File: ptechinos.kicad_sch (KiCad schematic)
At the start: 73 parts, among them J1 B+, J2 Battery, J3 B-, J4 AudioJack4, J5 Trackpad FPC, J6 OLED, SW1 SW_Power, SW2 Reset, U1 ProMicro

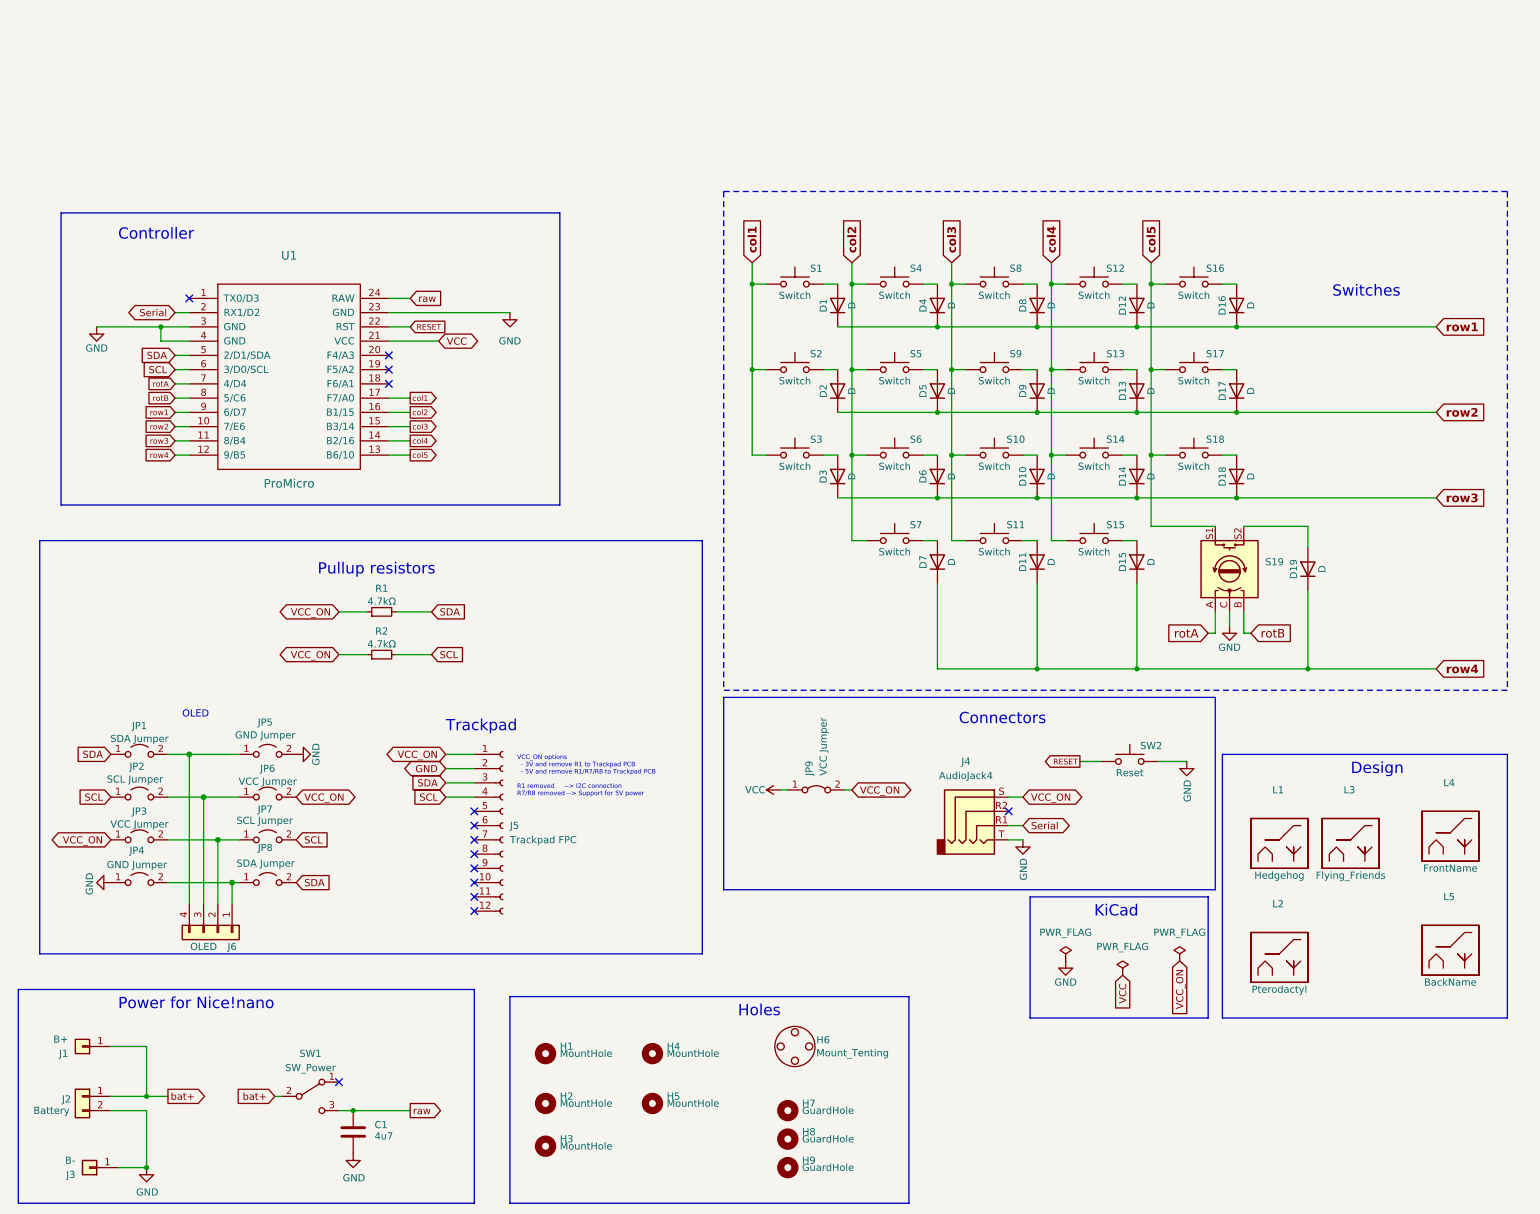
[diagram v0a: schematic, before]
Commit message: ✨ 💥 🚧 - Add another position for the encoder / key. Adjust matrix accordingly. Note that encoder A/B lines are currently shared. Update both schematic and PCB to fit all. Adjust board to 62c46e3cfa2ad35a7dbc6e8ceb0ca2087bb40a82 and 578a124142dade73bf22a96b8bd2c4353eafd8da.
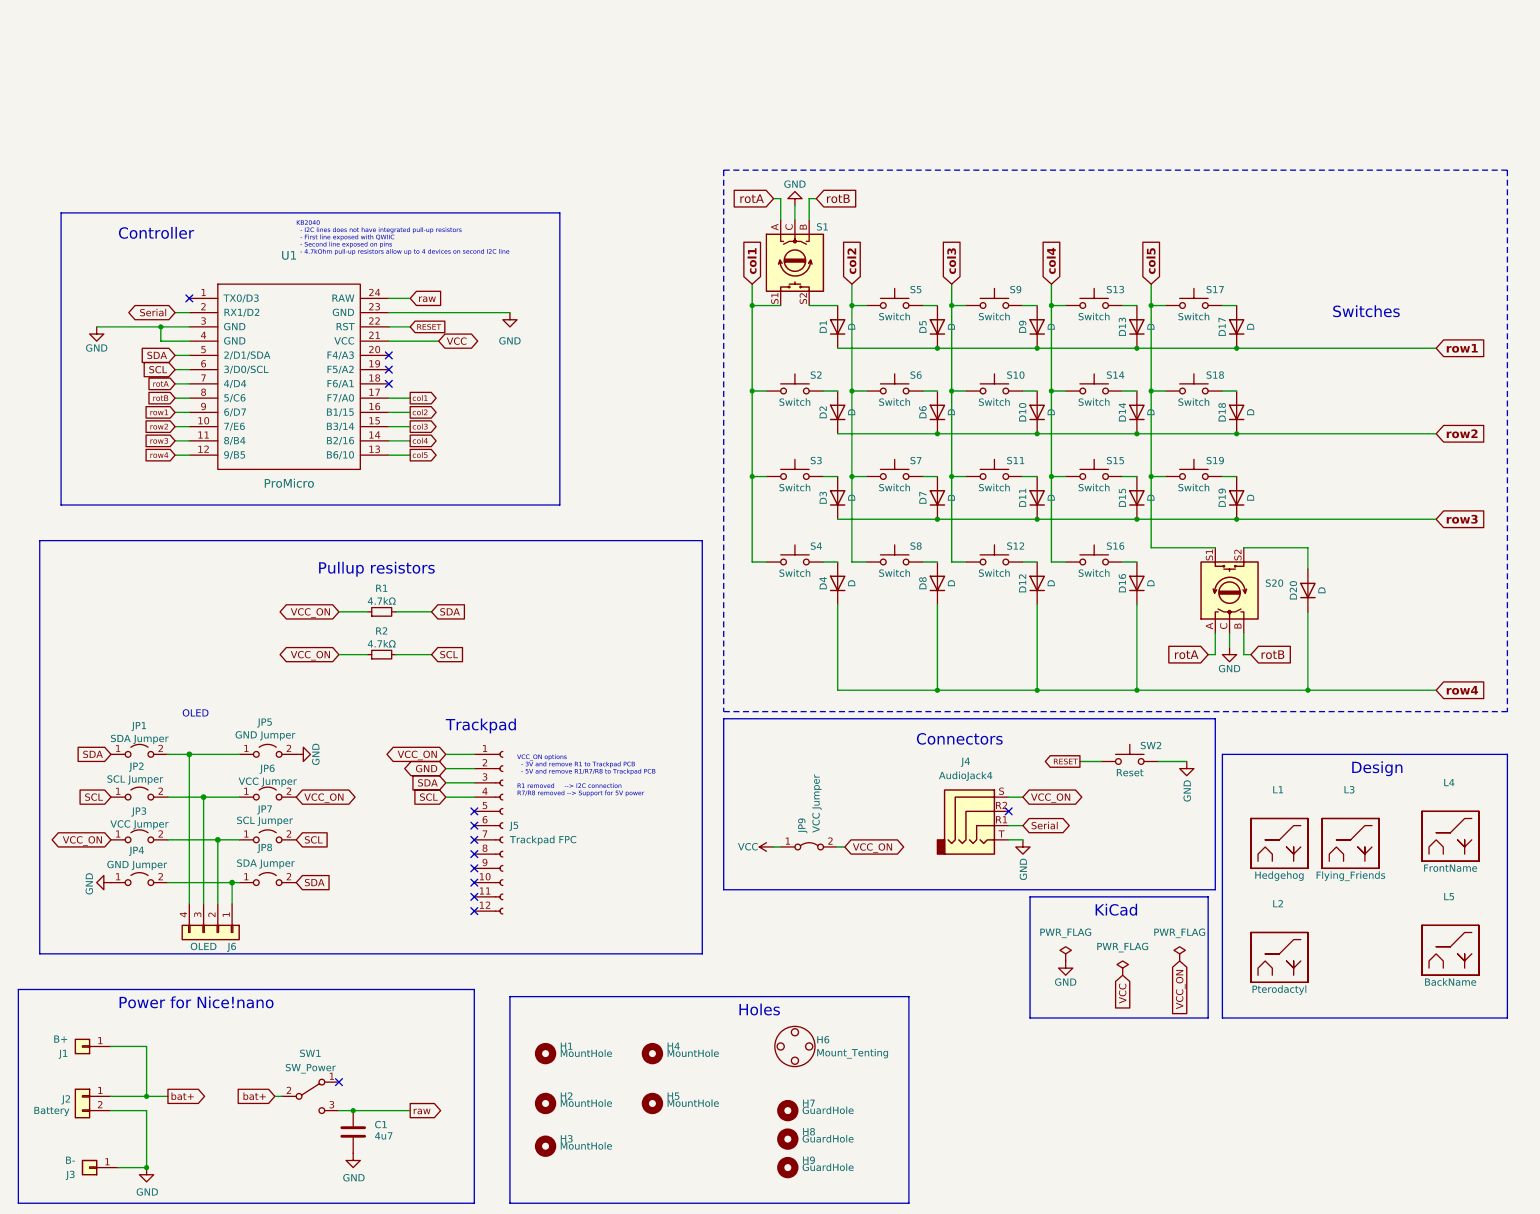
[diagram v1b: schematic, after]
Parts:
- removed S1: Switch, ptechinos:Kailh_socket_PG1350_optional_reversible.kicad_mod, symbol Switch:SW_Push
- added D4: D, ptechinos:D3_TH_SMD_v2, symbol Device:D
- added S1: RotaryEncoder_Switch, ptechinos:pg1350-EVQWGD001_R, symbol Device:RotaryEncoder_Switch
- added S4: Switch, ptechinos:Kailh_socket_PG1350_optional_reversible.kicad_mod, symbol Switch:SW_Push
- renumbered D9 to D10, D10 to D11, D11 to D12, D12 to D13, D13 to D14, D14 to D15, D15 to D16, D16 to D17, D17 to D18, D18 to D19, D19 to D20, D4 to D5, D5 to D6, D6 to D7, D7 to D8, D8 to D9, S9 to S10, S10 to S11, S11 to S12, S12 to S13, S13 to S14, S14 to S15, S15 to S16, S16 to S17, S17 to S18, S18 to S19, S19 to S20, S4 to S5, S5 to S6, S6 to S7, S7 to S8, S8 to S9
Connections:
- net GND: now also S1.C
- net col1: now also S1.S1, S4.1
- net rotA: now also S1.A
- net rotB: now also S1.B
- net row4: now also D4.1 (K)
- net at D1.2 (A): now also S1.S2
- new net: D4.2 (A), S4.2
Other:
- note added: "KB2040 - I2C lines does not have integrated pull-up resistors - First line exposed with QWIIC - Second line exposed on pins - 4.7kOhm pull-up resistors allow up to 4 devices on second I2C line"
- moved on the sheet: D1, D10, D11, D12, D13, D14, D15, D16, D17, D18, D19, D2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

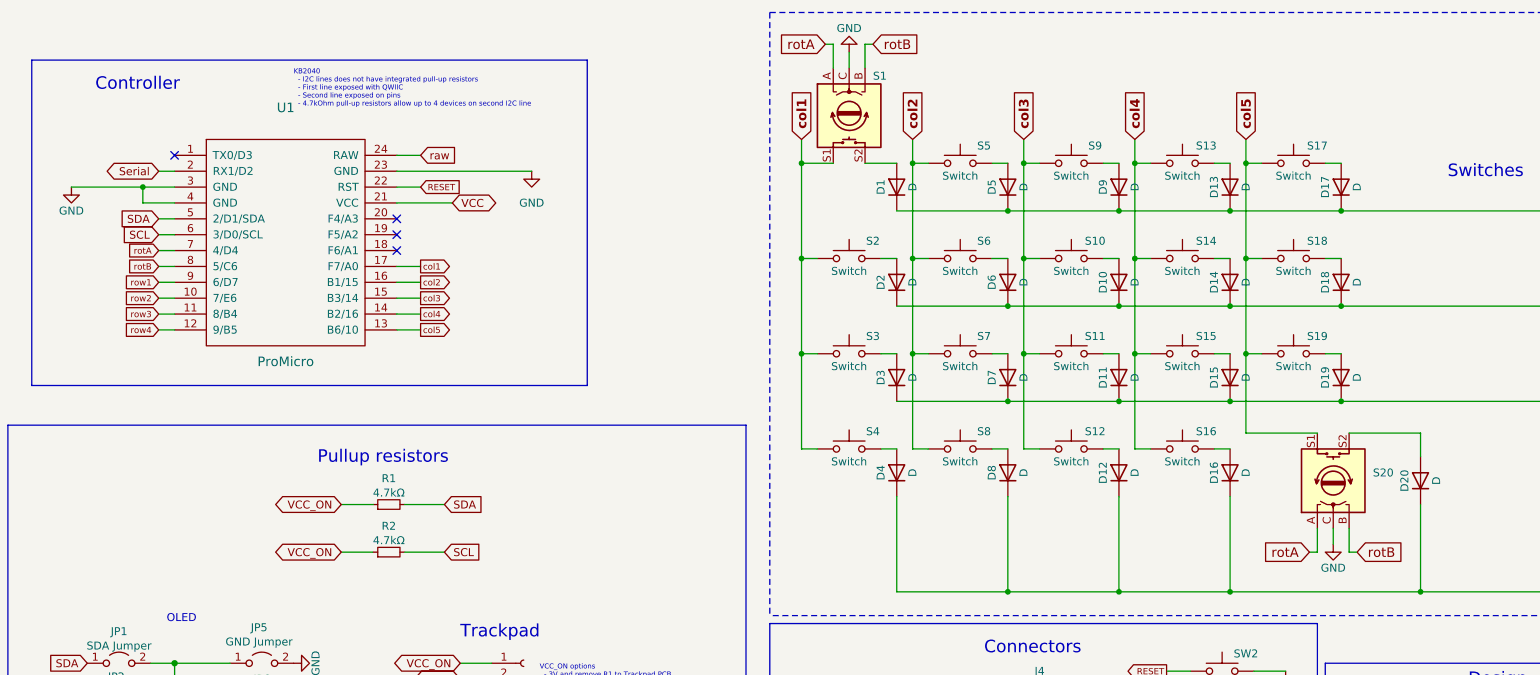
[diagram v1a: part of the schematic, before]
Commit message: ✨ 💥 - Both encoders (top and thumbs) are now using distinct pins.
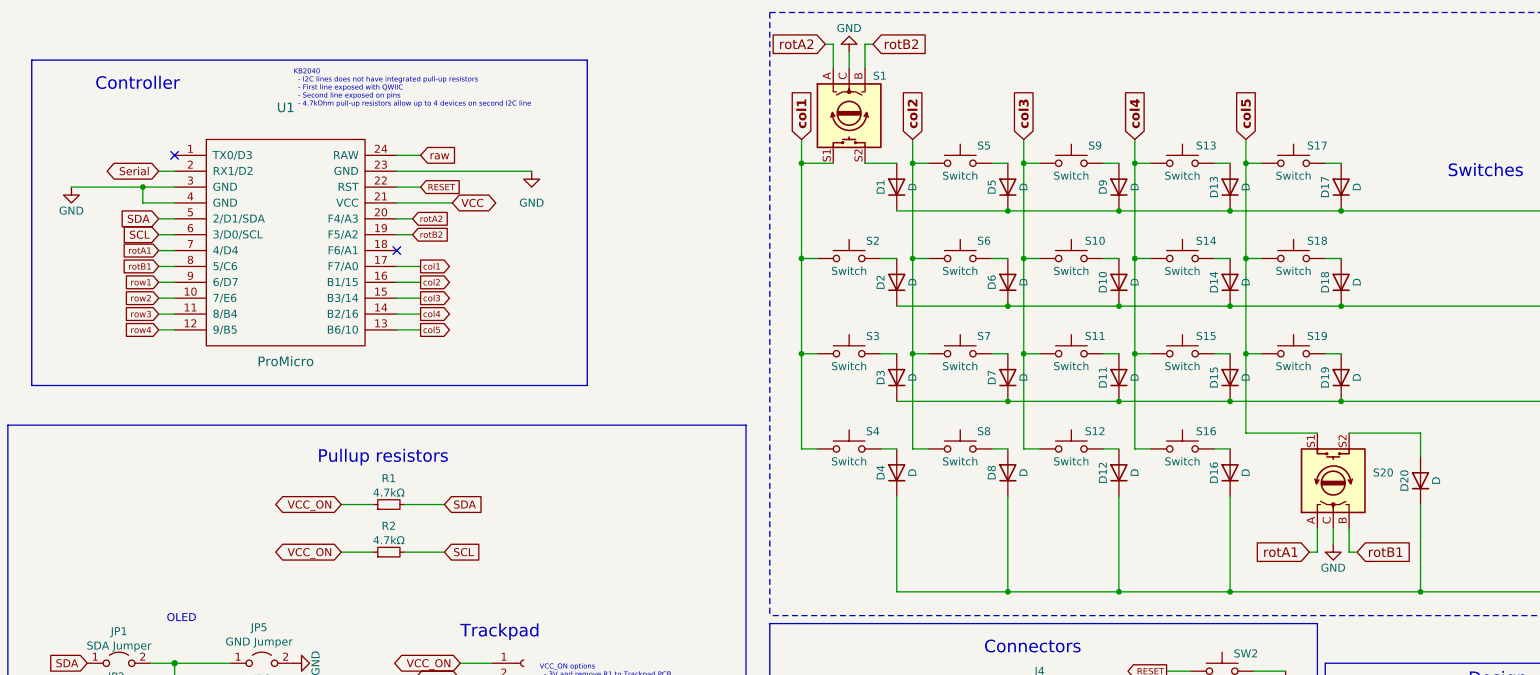
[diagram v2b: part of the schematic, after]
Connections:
- net rotB2: now reaches U1.19 (F5/A2)
- net rotB2: now also S1.B
- net rotA2: now reaches U1.20 (F4/A3)
- net rotA2: now also S1.A
- net rotA renamed rotA1
- net rotA1: no longer S1.A
- net rotB renamed rotB1
- net rotB1: no longer S1.B
- no-connect marks 14 -> 12
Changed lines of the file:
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@@
   (title_block
     (title "Ptechinos")
-    (date "2022-08-05")
+    (date "2022-08-14")
     (rev "0.6")
     (comment 1 "A crossover between Pteron36 and Balbuzard.")
@@
   (no_connect (at 95.25 142.24))
   (no_connect (at 95.25 139.7))
-  (no_connect (at 80.01 45.72))
   (no_connect (at 44.45 35.56))
   (no_connect (at 190.5 127))
@@
   (no_connect (at 95.25 127))
   (no_connect (at 95.25 129.54))
-  (no_connect (at 80.01 48.26))
   (no_connect (at 95.25 144.78))
   (no_connect (at 71.12 175.26))
@@
     (stroke (width 0) (type default) (color 0 0 0 0))
   )
+  (wire (pts (xy 82.55 45.72) (xy 80.01 45.72))
+    (stroke (width 0) (type default) (color 0 0 0 0))
+  )
   (wire (pts (xy 215.9 67.31) (xy 218.44 67.31))
     (stroke (width 0) (type default) (color 0 0 0 0))
@@
   )
   (wire (pts (xy 175.26 36.83) (xy 177.8 36.83))
+    (stroke (width 0) (type default) (color 0 0 0 0))
+  )
+  (wire (pts (xy 82.55 48.26) (xy 80.01 48.26))
     (stroke (width 0) (type default) (color 0 0 0 0))
   )
@@
     )
   )
-  (global_label "rotA" (shape input) (at 148.59 17.78 180) (fields_autoplaced)
+  (global_label "rotA2" (shape input) (at 148.59 17.78 180) (fields_autoplaced)
     (effects (font (size 1.524 1.524)) (justify right))
-    (property "Intersheet References" "${INTERSHEET_REFS}" (id 0) (at 141.195 17.6848 0)
+    (property "Intersheet References" "${INTERSHEET_REFS}" (id 0) (at 139.7435 17.6848 0)
       (effects (font (size 1.524 1.524)) (justify right) hide)
     )
@@
     )
   )
-  (global_label "rotA" (shape input) (at 226.06 99.06 180) (fields_autoplaced)
+  (global_label "rotA1" (shape input) (at 226.06 99.06 180) (fields_autoplaced)
     (effects (font (size 1.524 1.524)) (justify right))
-    (property "Intersheet References" "${INTERSHEET_REFS}" (id 0) (at 218.665 98.9648 0)
+    (property "Intersheet References" "${INTERSHEET_REFS}" (id 0) (at 217.2135 98.9648 0)
       (effects (font (size 1.524 1.524)) (justify right) hide)
     )
@@
     )
   )
-  (global_label "rotA" (shape input) (at 41.91 50.8 180) (fields_autoplaced)
+  (global_label "rotA1" (shape input) (at 41.91 50.8 180) (fields_autoplaced)
     (effects (font (size 1 1)) (justify right))
-    (property "Intersheet References" "${INTERSHEET_REFS}" (id 0) (at 37.0576 50.8625 0)
+    (property "Intersheet References" "${INTERSHEET_REFS}" (id 0) (at 36.1052 50.7375 0)
       (effects (font (size 1 1)) (justify right) hide)
     )
@@
     )
   )
-  (global_label "rotB" (shape input) (at 233.68 99.06 0) (fields_autoplaced)
+  (global_label "rotB2" (shape input) (at 82.55 48.26 0) (fields_autoplaced)
+    (effects (font (size 1 1)) (justify left))
+    (property "Intersheet References" "${INTERSHEET_REFS}" (id 0) (at 88.4976 48.1975 0)
+      (effects (font (size 1 1)) (justify left) hide)
+    )
+  )
+  (global_label "rotB1" (shape input) (at 233.68 99.06 0) (fields_autoplaced)
     (effects (font (size 1.524 1.524)) (justify left))
-    (property "Intersheet References" "${INTERSHEET_REFS}" (id 0) (at 241.2927 98.9648 0)
+    (property "Intersheet References" "${INTERSHEET_REFS}" (id 0) (at 242.7442 98.9648 0)
       (effects (font (size 1.524 1.524)) (justify left) hide)
     )
@@
     )
   )
-  (global_label "rotB" (shape input) (at 156.21 17.78 0) (fields_autoplaced)
+  (global_label "rotB2" (shape input) (at 156.21 17.78 0) (fields_autoplaced)
     (effects (font (size 1.524 1.524)) (justify left))
-    (property "Intersheet References" "${INTERSHEET_REFS}" (id 0) (at 163.8227 17.6848 0)
+    (property "Intersheet References" "${INTERSHEET_REFS}" (id 0) (at 165.2742 17.6848 0)
       (effects (font (size 1.524 1.524)) (justify left) hide)
     )
@@
     )
   )
-  (global_label "rotB" (shape input) (at 41.91 53.34 180) (fields_autoplaced)
+  (global_label "rotB1" (shape input) (at 41.91 53.34 180) (fields_autoplaced)
     (effects (font (size 1 1)) (justify right))
-    (property "Intersheet References" "${INTERSHEET_REFS}" (id 0) (at 36.9148 53.4025 0)
+    (property "Intersheet References" "${INTERSHEET_REFS}" (id 0) (at 35.9624 53.2775 0)
       (effects (font (size 1 1)) (justify right) hide)
     )
@@
       (effects (font (size 1 1)) (justify left) hide)
     )
+  )
+  (global_label "rotA2" (shape input) (at 82.55 45.72 0) (fields_autoplaced)
+    (effects (font (size 1 1)) (justify left))
+    (property "Intersheet References" "${INTERSHEET_REFS}" (id 0) (at 88.3548 45.6575 0)
+      (effects (font (size 1 1)) (justify left) hide)
+    )
